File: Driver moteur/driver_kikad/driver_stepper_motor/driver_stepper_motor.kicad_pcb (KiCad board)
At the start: 2 copper layers, 67 x 58 mm, 52 parts, among them U1 STM32G031G8U6

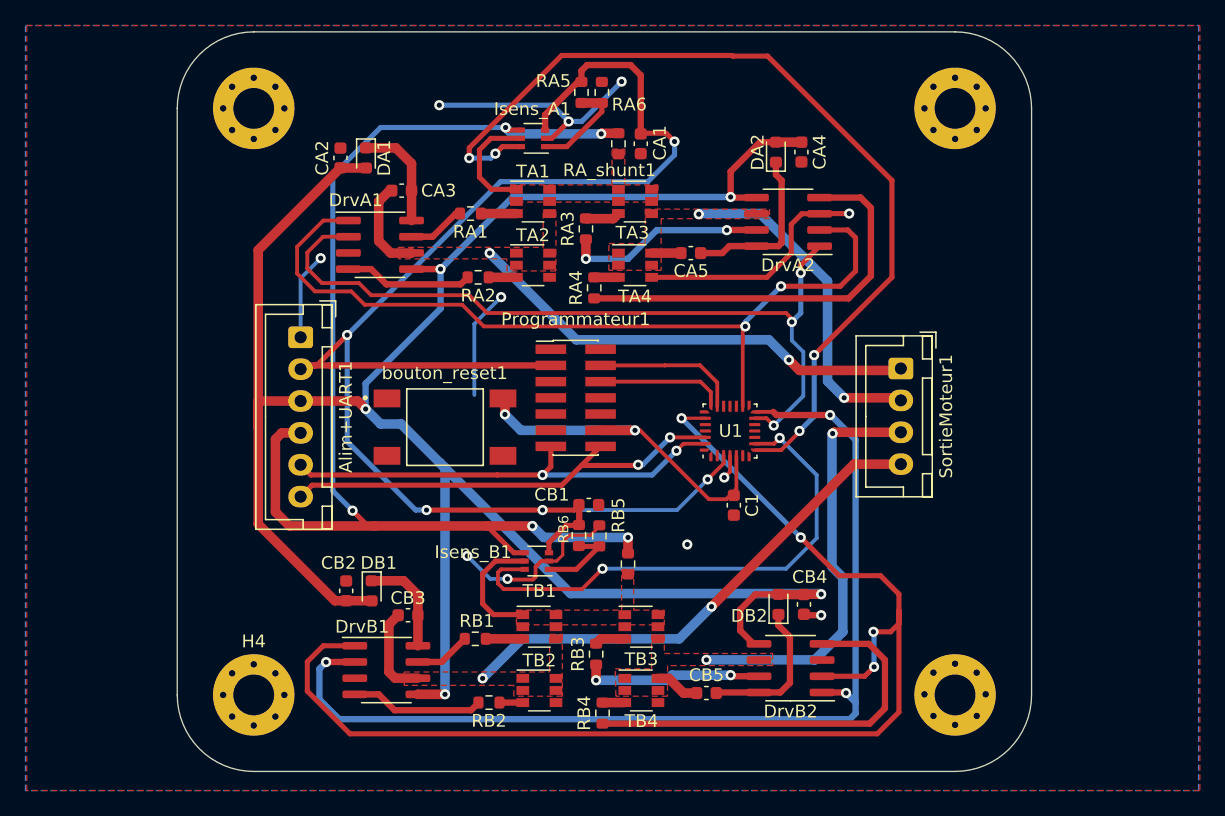
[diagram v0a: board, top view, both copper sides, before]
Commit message: ajout du nom et augmentation des traces
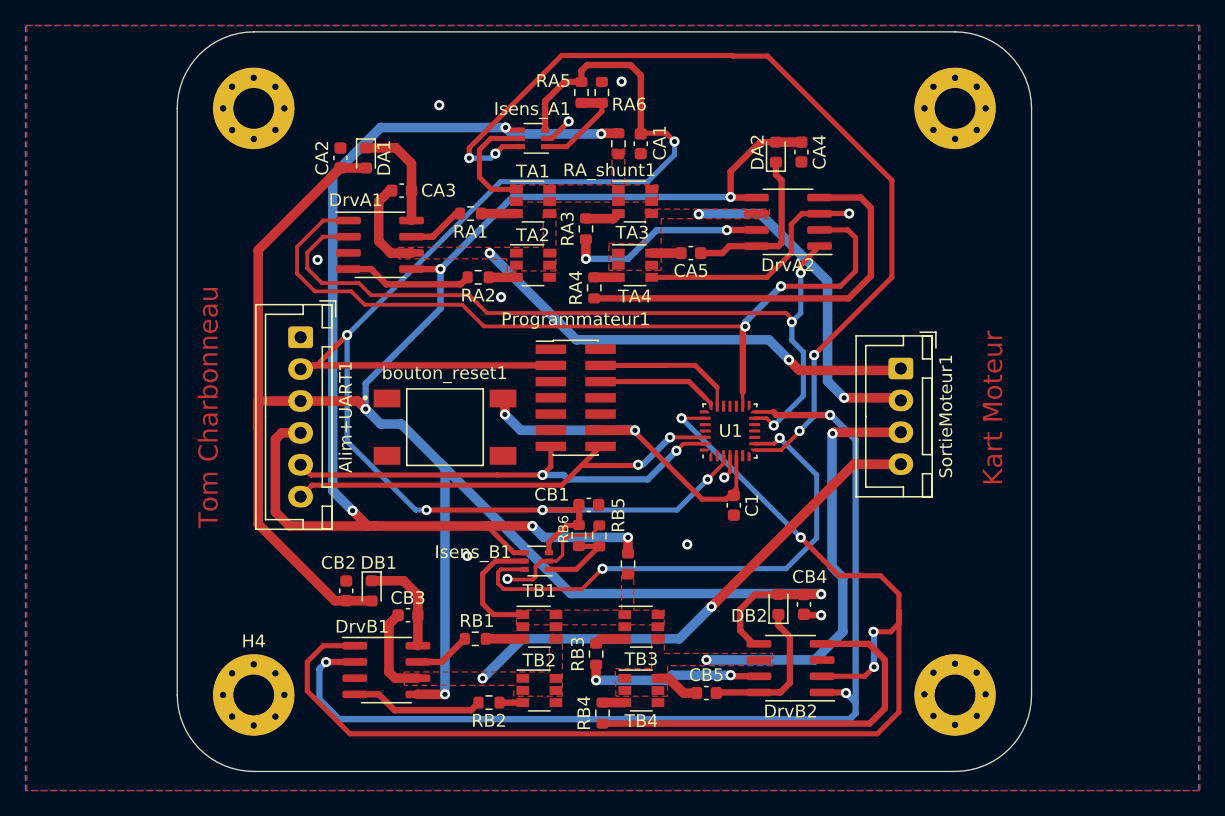
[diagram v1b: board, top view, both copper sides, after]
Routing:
- net GND: track 70.1 -> 34.7 mm
- net 3,3V: track 125.1 -> 125.7 mm
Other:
- rule pad_to_mask_clearance: 0 -> 0.1
- board text added: "Kart Moteur"
- board text added: "Tom Charbonneau"
